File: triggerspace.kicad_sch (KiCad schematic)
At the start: 139 parts, among them J1 Conn_01x2, J10 Conn_01x12, J11 Conn_01x12, J12 Conn_02x05_Odd_Even, J13 Conn_01x10, J14 Conn_01x10, J15 Conn_01x10, J2 Conn_01x2, J3 Conn_01x4, J4 Conn_01x4, J5 Conn_01x3, J6 Conn_01x3, J7 Conn_01x10, J8 Conn_01x3, J9 Conn_01x2, Q1 2N3904, Q2 2N3904, U1 MCP6002_1, U2 MCP6002_1, U3 MCP6002_1, U4 L7805, U5 LM4040LP-5, U6 74HC595, U8 HCPL-2630, U9 HCPL-0630, X1 CV_X, Y1 CV_Y

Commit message: D8: optional 5.1V zener footprint as an alternative to U5 (LM4040LP-5)
Upright DO-35 footprint inside U5's outline, cathode to GND, anode on the
-5V ref_5 rail; ref_5 re-routed locally around it. README build option and
CHANGELOG entry.
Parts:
- added D8: 5.1V, Diode_THT:D_DO-35_SOD27_P2.54mm_Vertical_KathodeUp, symbol Device:D_Zener
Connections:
- net GND: now also D8.1 (K)
- net ref_5: now also D8.2 (A)
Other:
- note added: "Fit U5 (LM4040LP-5) OR D8 (5.1V zener), not both."
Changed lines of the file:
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@@
+		)
+	)
+	(symbol
+		(lib_id "Device:D_Zener")
+		(at 223.52 85.09 90)
+		(unit 1)
+		(exclude_from_sim no)
+		(in_bom yes)
+		(on_board yes)
+		(dnp yes)
+		(property "Reference" "D8"
+			(at 220.98 83.82 270)
+			(effects
+				(font
+					(size 1.27 1.27)
+				)
+				(justify right)
+			)
+		)
+		(property "Value" "5.1V"
+			(at 220.98 86.36 270)
+			(effects
+				(font
+					(size 1.27 1.27)
+				)
+				(justify right)
+			)
+		)
+		(property "Footprint" "Diode_THT:D_DO-35_SOD27_P2.54mm_Vertical_KathodeUp"
+			(at 223.52 85.09 0)
+			(effects
+				(font
+					(size 1.27 1.27)
+				)
+				(hide yes)
+			)
+		)
+		(property "Datasheet" "~"
+			(at 223.52 85.09 0)
+			(effects
+				(font
+					(size 1.27 1.27)
+				)
+				(hide yes)
+			)
+		)
+		(property "Description" "Zener diode"
+			(at 223.52 85.09 0)
+			(effects
+				(font
+					(size 1.27 1.27)
+				)
+				(hide yes)
+			)
+		)
+		(pin "1"
+		)
+		(pin "2"
+		)
+		(instances
+			(project "triggerspace"
+				(path "/a5cd8da1-8f7f-4f80-bb23-0317de562222"
+					(reference "D8")
+					(unit 1)
+				)
+			)
+		)
+	)
+	(symbol
+		(lib_id "NanoGris-rescue:GND-power-GridsNanoV3-rescue")
+		(at 223.52 93.98 0)
+		(unit 1)
+		(exclude_from_sim no)
+		(in_bom yes)
+		(on_board yes)
+		(dnp no)
+		(property "Reference" "#PWR0172"
+			(at 223.52 100.33 0)
+			(effects
+				(font
+					(size 1.27 1.27)
+				)
+				(hide yes)
+			)
+		)
+		(property "Value" "GND"
+			(at 223.52 97.79 0)
+			(effects
+				(font
+					(size 1.27 1.27)
+				)
+			)
+		)
+		(property "Footprint" ""
+			(at 223.52 93.98 0)
+			(effects
+				(font
+					(size 1.27 1.27)
+				)
+				(hide yes)
+			)
+		)
+		(property "Datasheet" ""
+			(at 223.52 93.98 0)
+			(effects
+				(font
+					(size 1.27 1.27)
+				)
+				(hide yes)
+			)
+		)
+		(property "Description" ""
+			(at 223.52 93.98 0)
+			(effects
+				(font
+					(size 1.27 1.27)
+				)
+				(hide yes)
+			)
+		)
+		(pin "1"
+		)
+		(instances
+			(project "triggerspace"
+				(path "/a5cd8da1-8f7f-4f80-bb23-0317de562222"
+					(reference "#PWR0172")
+					(unit 1)
+				)
+			)
 		)
 	)
@@
 		(effects
 			(font
+				(size 1.27 1.27)
+			)
+			(justify left bottom)
+		)
+	)
+	(wire
+		(pts
+			(xy 223.52 81.28) (xy 223.52 77.47)
+		)
+		(stroke
+			(width 0)
+			(type default)
+		)
+	)
+	(wire
+		(pts
+			(xy 223.52 77.47) (xy 226.06 77.47)
+		)
+		(stroke
+			(width 0)
+			(type default)
+		)
+	)
+	(global_label "ref_5"
+		(shape bidirectional)
+		(at 226.06 77.47 0)
+		(fields_autoplaced yes)
+		(effects
+			(font
+				(size 1.27 1.27)
+			)
+			(justify left)
+		)
+		(property "Intersheetrefs" "${INTERSHEET_REFS}"
+			(at 226.06 77.47 0)
+			(effects
+				(font
+					(size 1.27 1.27)
+				)
+				(justify left)
+				(hide yes)
+			)
+		)
+	)
+	(wire
+		(pts
+			(xy 223.52 88.9) (xy 223.52 93.98)
+		)
+		(stroke
+			(width 0)
+			(type default)
+		)
+	)
+	(text "Fit U5 (LM4040LP-5) OR D8 (5.1V zener), not both."
+		(exclude_from_sim no)
+		(at 196.85 102.87 0)
+		(effects
+			(font

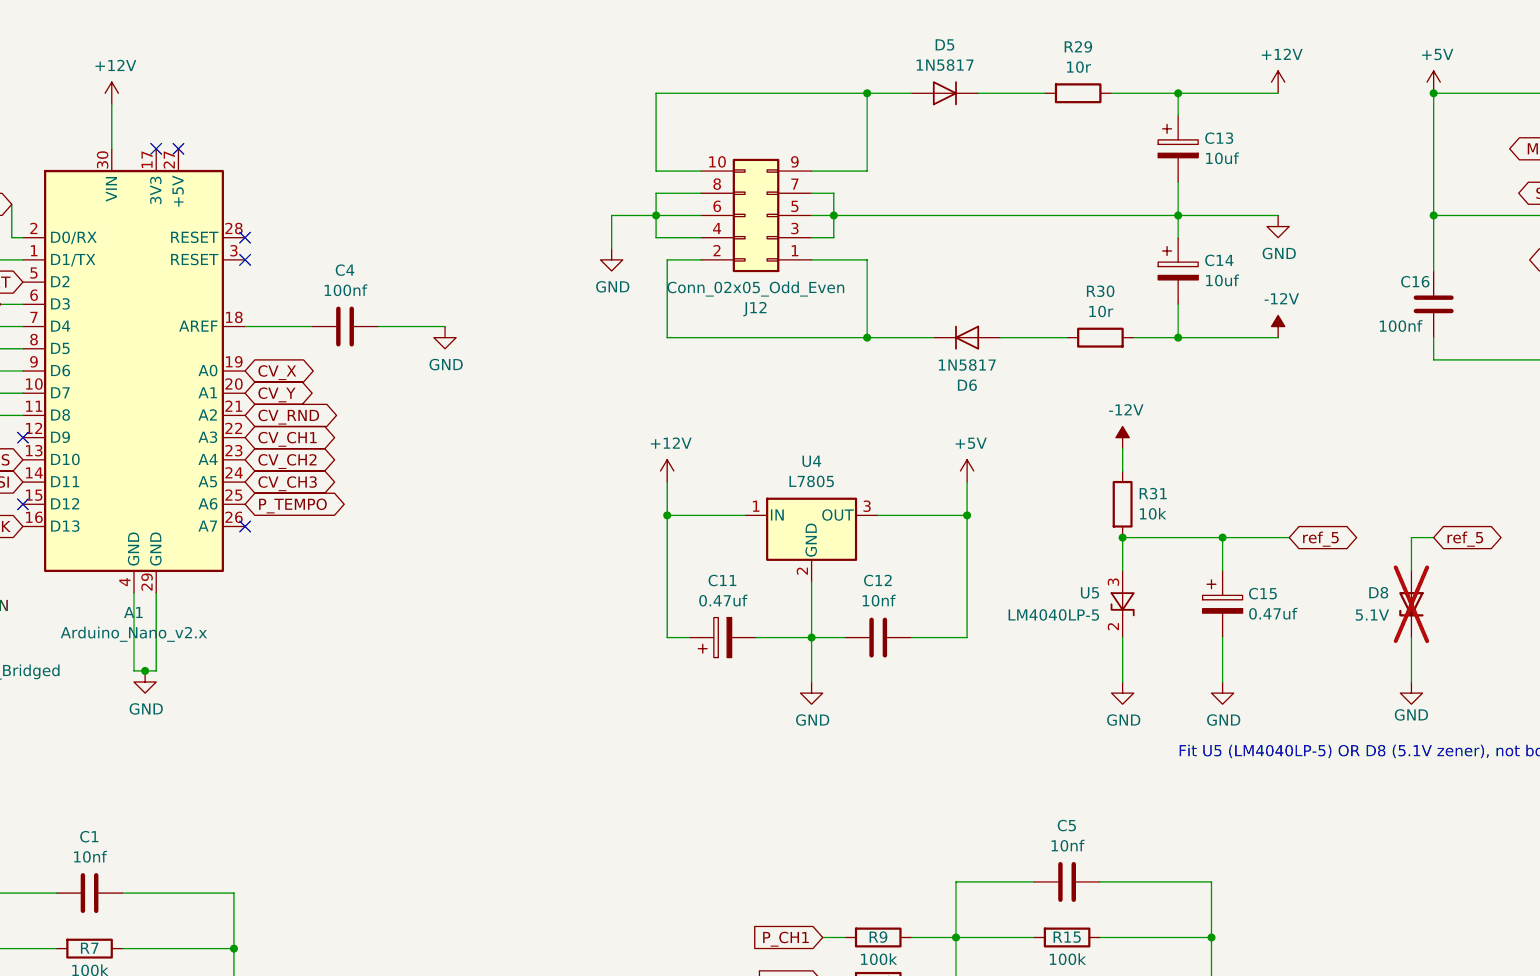
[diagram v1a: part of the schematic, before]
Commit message: +5V supply options: JP5 (Nano regulator), JP6 (Eurorack +5V), 16-pin J12
- JP5 (open) links the Nano's 5V pin (A1 pin 27) to the +5V rail
- J12 becomes a 2x8 footprint (a 2x5 header still fits pins 1-10); pins 11/12
  (Eurorack +5V) reach the +5V rail through JP6 (open), pins 13-16 unconnected
- U4, C11, C12 marked OPTIONAL on the silkscreen
- D5 moved left, R29 upright (2.54mm), power tracks around J12 re-routed;
  zones refilled with the project's rules
- README: +5V supply build option, JP5/JP6 in Jumpers, updated back PCB diagram;
  CHANGELOG entries
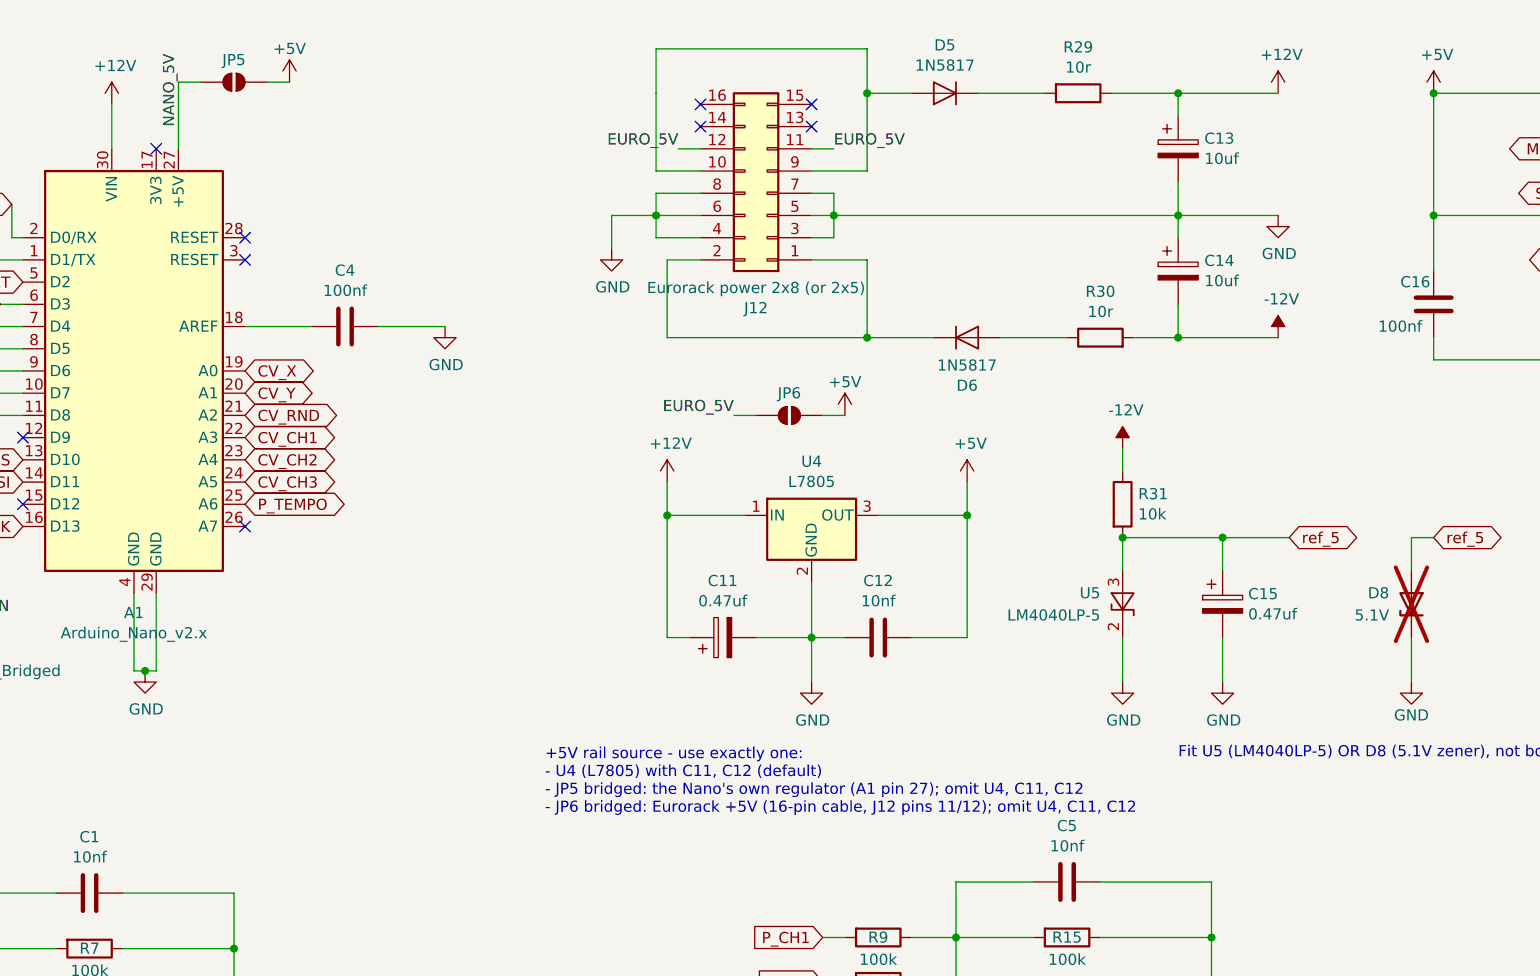
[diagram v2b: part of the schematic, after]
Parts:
- added JP5, JP6: SolderJumper_2_Open, Jumper:SolderJumper-2_P1.3mm_Open_RoundedPad1.0x1.5mm, symbol Jumper:SolderJumper_2_Open
- J12: value Conn_02x05_Odd_Even -> Eurorack power 2x8 (or 2x5); footprint Connector_IDC:IDC-Header_2x05_P2.54mm_Vertical -> Connector_IDC:IDC-Header_2x08_P2.54mm_Vertical; symbol NanoGris-rescue:Conn_02x05_Odd_Even-Connector_Generic-GridsNanoV3-rescue -> Connector_Generic:Conn_02x08_Odd_Even
- R29: footprint Resistor_THT:R_Axial_DIN0204_L3.6mm_D1.6mm_P7.62mm_Horizontal -> Resistor_THT:R_Axial_DIN0204_L3.6mm_D1.6mm_P2.54mm_Vertical
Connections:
- net +5V: now also JP5.2 (B), JP6.2 (B)
- net NANO_5V: now reaches A1.27 (+5V)
- net NANO_5V: now also JP5.1 (A)
- new net EURO_5V: J12.11 (Pin_11), J12.12 (Pin_12), JP6.1 (A)
- no-connect marks 8 -> 11
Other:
- note added: "+5V rail source - use exactly one: - U4 (L7805) with C11, C12 (default) - JP5 bridged: the Nano's own regulator (A1 pin 27); omit U4, C11, C12 - JP6 bridged: Eurorack +5V (16-pin cable, J12 pins 11/12); omit U4, C11, C12"
